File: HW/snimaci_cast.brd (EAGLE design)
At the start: 99 x 72.1 mm, 76 parts, among them K1 G5LE, K2 G5LE, Q1 2N7002, Q3 2N7002

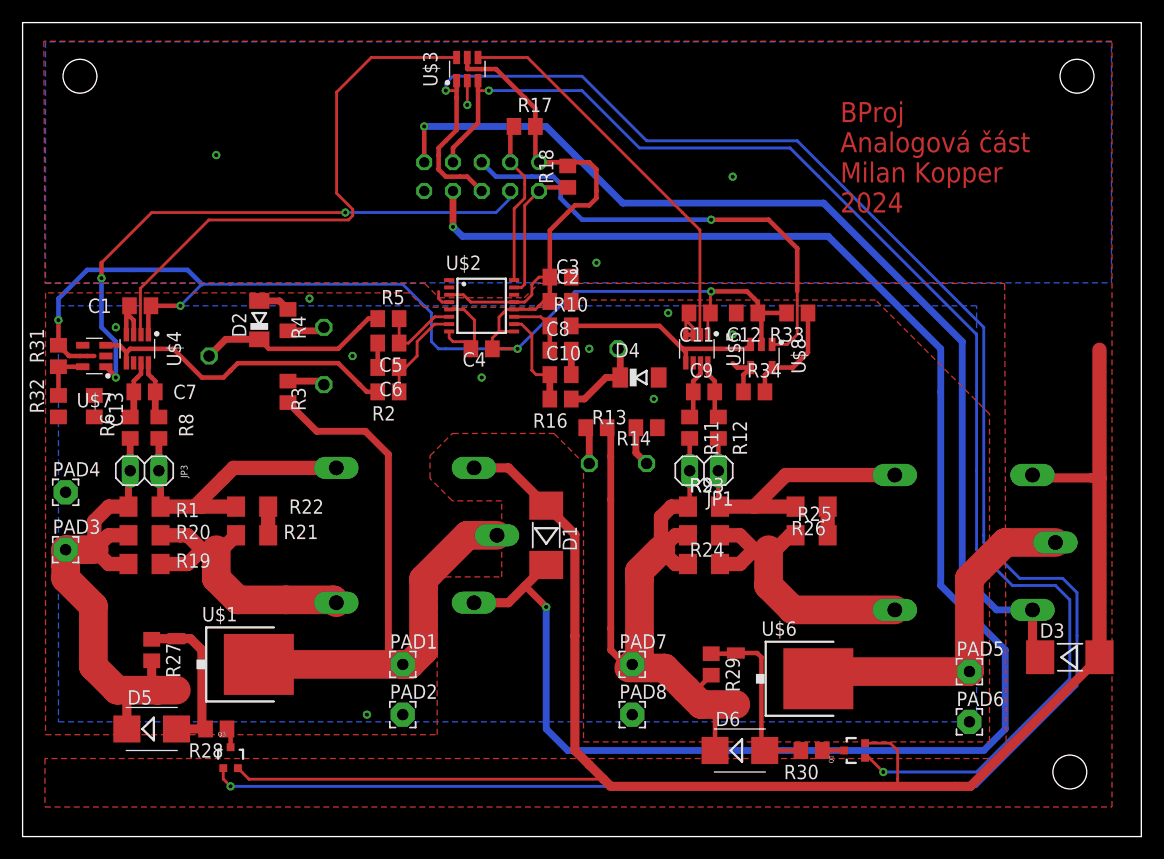
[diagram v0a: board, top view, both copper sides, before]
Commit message: Přidáno propojení desek fastony a distančními sloupky, změněna logika vyhodnocení nežádoucích stavů
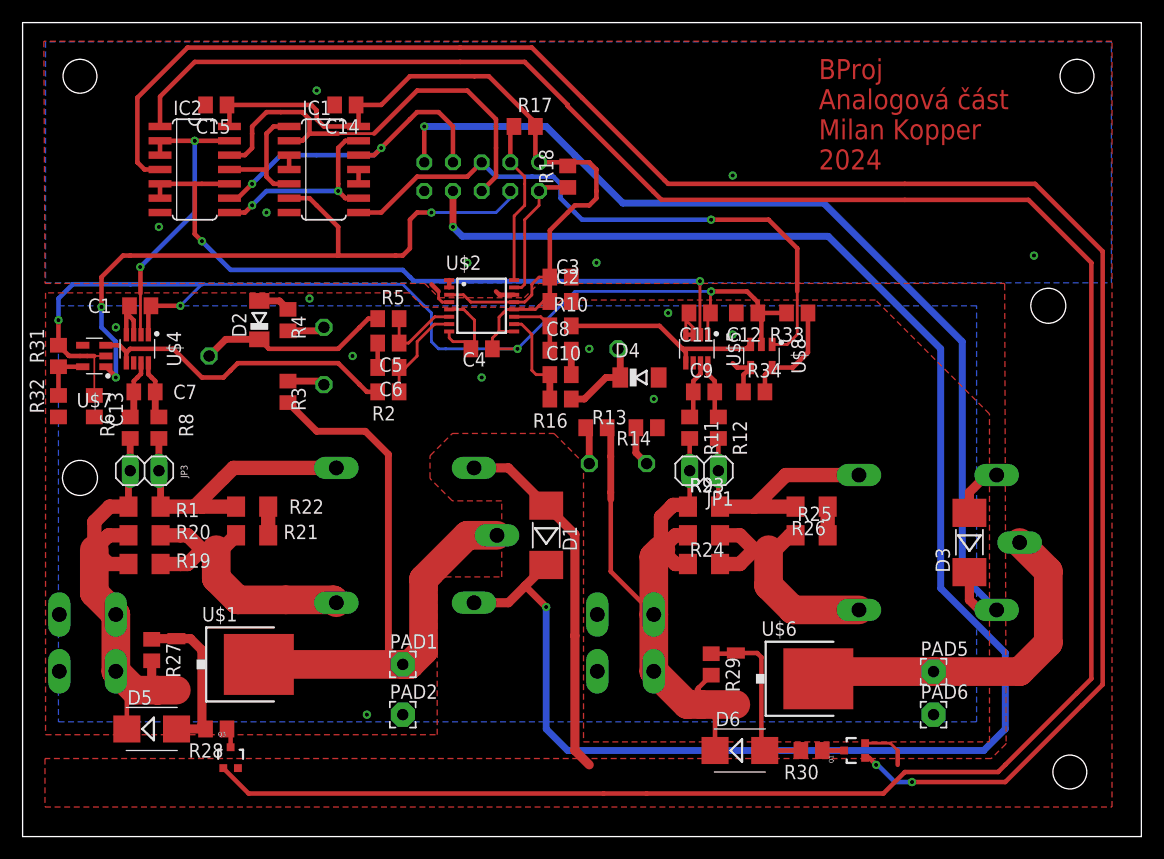
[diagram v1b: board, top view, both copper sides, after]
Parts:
- removed PAD3, PAD4, PAD7, PAD8: (no value), wirepad:2,15/1,0
- removed U$3: SN74LVC2GU04, TI_logic:SOT23-6
- added C14, C15: u1, rcl:C0805
- added IC1, IC2: 7402D, 74xx-eu:SO14
- added X1, X2: (no value), con-rib:SH5-2
- moved D3 13.5 mm to (114.3, 38.1), turned to 90 degrees
- moved PAD6 3.24 mm to (111.1, 22.9)
- moved K2 3.17 mm to (109.2, 38.1)
- moved PAD5 3.17 mm to (111.1, 26.7)
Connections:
- new net N$24: IC1.3, IC1.4
- new net N$26: IC1.10, IC1.11
- new net Q_1: IC1.1, IC1.5, IC2.11
- new net Q_2: IC1.13, IC1.9, IC2.8
- new net ZKRATOVANI_1: IC2.1, Q3.1
- new net ZKRATOVANI_2: IC2.4, Q1.1
- net +3V3: now also C14.1, C15.1, IC1.14, IC2.14; no longer U$3.5
- net A1_IN: now also X1.1, X1.2; no longer PAD3.1
- net A2_IN: now also X2.1, X2.2; no longer PAD7.1
- net AGND: now also X1.3, X1.4, X2.3, X2.4; no longer PAD4.1, PAD8.1
- net EN1: now also IC2.13, IC2.2, IC2.3; no longer U$3.6
- net EN2: now also IC2.10, IC2.5, IC2.6; no longer U$3.4
- net GND: now also C14.2, C15.2, IC1.7, IC2.7; no longer U$3.2
- net INT1: now also IC1.6
- net INT2: now also IC1.8
- net PROT1: now also IC1.2, IC2.12; no longer Q3.1, U$3.1
- net PROT2: now also IC1.12, IC2.9; no longer Q1.1, U$3.3
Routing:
- net ZKRATOVANI_1: track 0.00 -> 212.6 mm
- net ZKRATOVANI_2: track 0.00 -> 166.6 mm, vias 0 -> 2
- net PROT1: track 189.7 -> 39.4 mm, vias 2 -> 0
- net GND: track 159.2 -> 46.6 mm, vias 4 -> 7
- net PROT2: track 119.4 -> 28.9 mm
- net +3V3: track 150.9 -> 181.5 mm
- net EN2: track 35.3 -> 63.1 mm, vias 0 -> 2
- net EN1: track 49.0 -> 26.6 mm, vias 0 -> 2
- net Q_2: track 0.00 -> 18.4 mm, vias 0 -> 2
- net INT2: track 42.0 -> 54.8 mm
- net Q_1: track 0.00 -> 11.6 mm
- net INT1: track 51.2 -> 59.9 mm
- net A2_IN: track 71.0 -> 64.5 mm
- net A1_IN: track 47.8 -> 43.4 mm
- net N$6: track 26.4 -> 23.2 mm
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
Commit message: Verze zadaná do výroby
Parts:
- added R35: (no value), rcl:R0805
- C1, C11, C14, C15: value u1 -> 100n
- C10, C2, C3, C4, C5, C6, C7, C8, C9: value (none) -> 100n
- R10, R16, R2, R5: value (none) -> 1K
- R11, R12, R6, R8: value (none) -> 550R
- R13: value (none) -> 15K
- R14: value (none) -> 820R
- R15: value (none) -> 500R
- R17, R18: value (none) -> 5K
- moved C13 7.90 mm to (36.2, 58.0), turned to 180 degrees
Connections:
- net AGND: now also R35.1
- net GND: now also R35.2
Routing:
- net AGND: track 27.9 -> 49.6 mm, vias 9 -> 14
- net GND: track 46.6 -> 60.3 mm, vias 7 -> 10
- net ZKRATOVANI_1: track 212.6 -> 201.7 mm
- net ZKRATOVANI_2: track 166.6 -> 156.3 mm
- net +3V3: track 181.5 -> 173.4 mm
- net A2_IN: track 64.5 -> 63.1 mm
- net INT1: track 59.9 -> 58.6 mm
- net RELE1: vias 2 -> 4
- net RELE2: vias 1 -> 3
- removed copper zone on layer 1, net AGND
- removed copper zone on layer 1, net GND
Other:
- board text added: "Snímací deska Milan Kopper 2024 v1.0"
- board text removed: "BProj Analogová část Milan Kopper 2024"
